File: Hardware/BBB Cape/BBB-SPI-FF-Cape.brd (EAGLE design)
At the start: 72.1 x 90.2 mm, 10 parts

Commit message: created the images for the modela
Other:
- board size 72.1 x 90.2 mm -> 54.6 x 71.8 mm

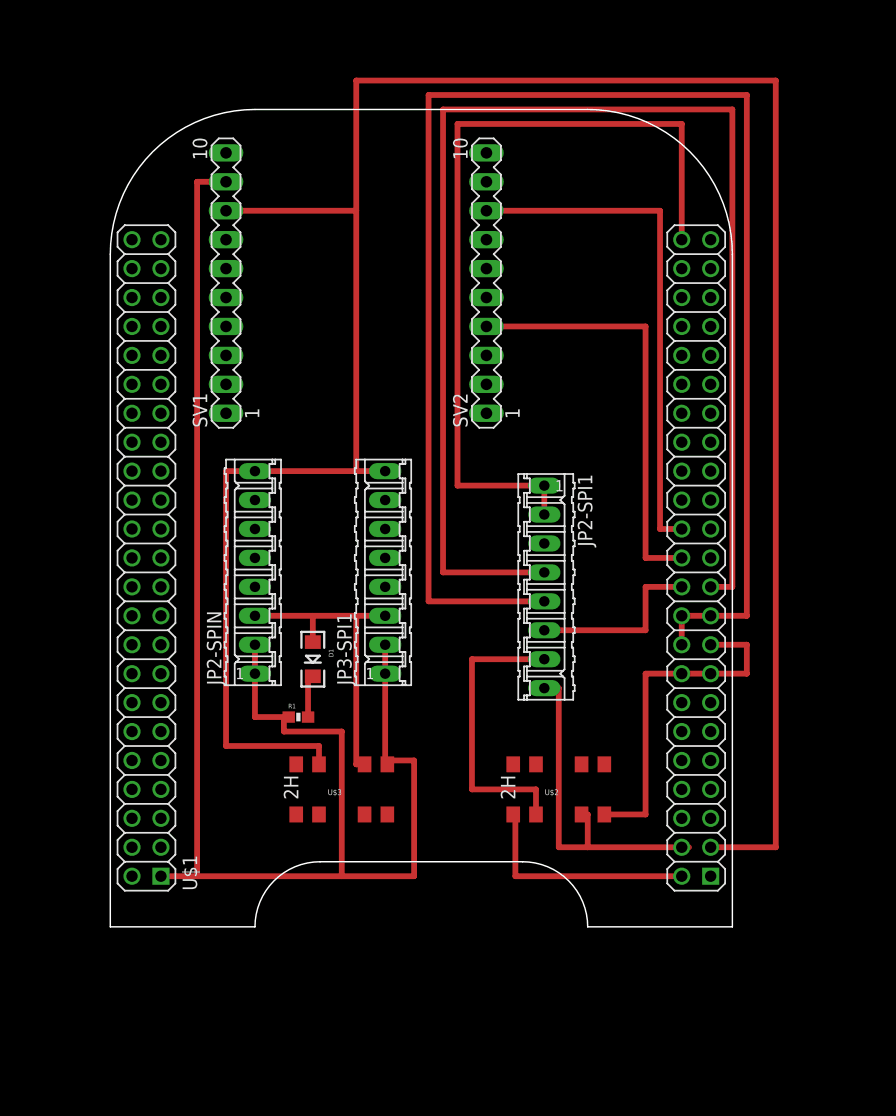
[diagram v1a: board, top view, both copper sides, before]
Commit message: Fixed the headers for the M08 cables coming from the IMU
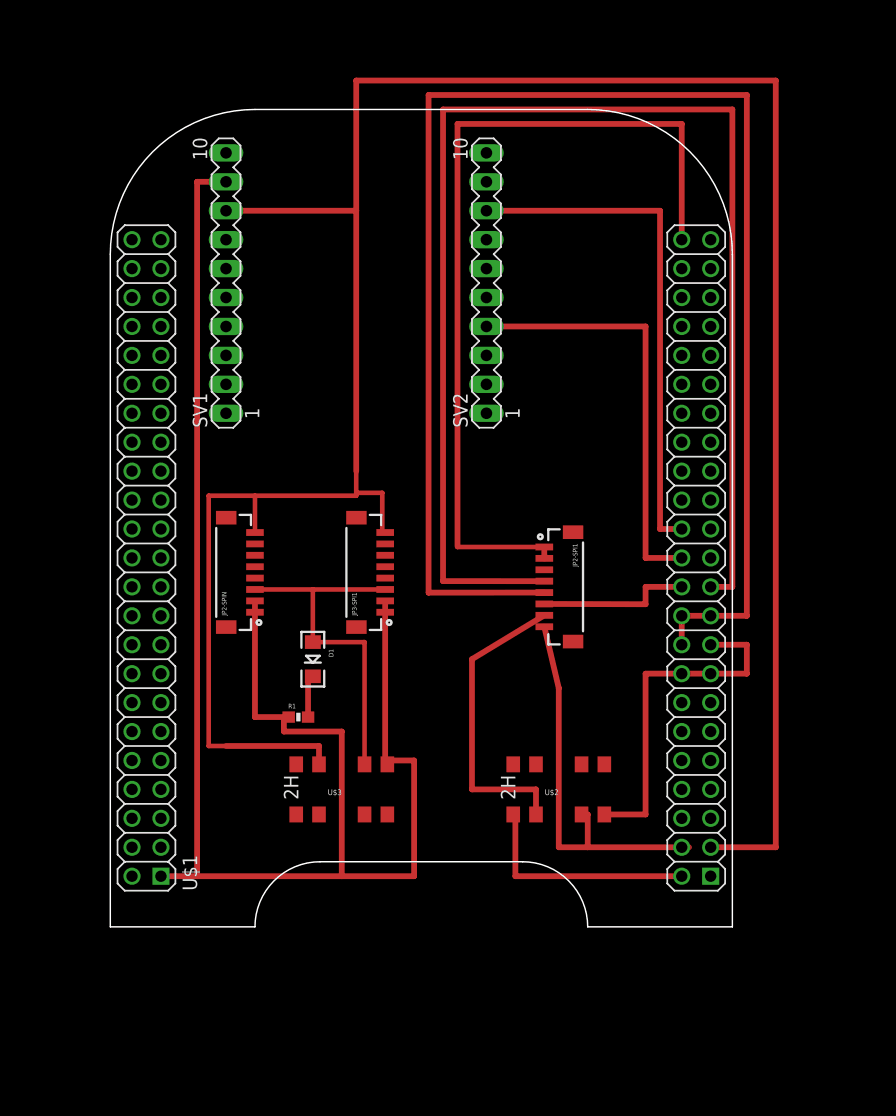
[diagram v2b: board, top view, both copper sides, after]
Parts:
- JP2-SPI1, JP2-SPIN, JP3-SPI1: device con-amp-quick:08P -> SparkFun-Connectors:BM08B-SRSS-TB
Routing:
- net GND: track 229.1 -> 240.7 mm
- net VCC: track 203.4 -> 213.2 mm
- net N$3: track 30.1 -> 34.4 mm
- net D: track 27.5 -> 31.3 mm
- net SCL: track 15.9 -> 13.6 mm
- net FF-CLK: track 25.9 -> 27.0 mm
- net SDO: track 118.7 -> 119.5 mm
- net SDA: track 136.5 -> 135.8 mm

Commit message: Cleaned up some of the traces
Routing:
- net FF-CLK: track 27.0 -> 29.8 mm
- net N$3: track 34.4 -> 35.5 mm
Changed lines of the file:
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@@
 <contactref element="JP2-SPI1" pad="8"/>
 <contactref element="U$2" pad="6"/>
-<wire x1="45.72" y1="39.68" x2="46.99" y2="34.29" width="0.508" layer="1"/>
 <wire x1="46.99" y1="34.29" x2="46.99" y2="20.32" width="0.508" layer="1"/>
 <wire x1="46.99" y1="20.32" x2="49.53" y2="20.32" width="0.508" layer="1"/>
@@
 <wire x1="48.99" y1="23.2" x2="49.53" y2="23.2" width="0.508" layer="1"/>
 <wire x1="49.53" y1="23.2" x2="49.53" y2="20.32" width="0.508" layer="1"/>
+<wire x1="45.72" y1="39.68" x2="45.72" y2="34.417" width="0.4064" layer="1"/>
+<wire x1="45.72" y1="34.417" x2="46.99" y2="34.417" width="0.4064" layer="1"/>
+<wire x1="46.99" y1="34.417" x2="46.99" y2="34.29" width="0.4064" layer="1"/>
 </signal>
 <signal name="D">
@@
 <contactref element="U$2" pad="7"/>
 <wire x1="44.99" y1="22.86" x2="44.99" y2="23.2" width="0.508" layer="1"/>
-<wire x1="45.72" y1="40.68" x2="39.37" y2="36.83" width="0.508" layer="1"/>
-<wire x1="39.37" y1="36.83" x2="39.37" y2="25.4" width="0.508" layer="1"/>
+<wire x1="45.72" y1="40.68" x2="39.37" y2="40.64" width="0.508" layer="1"/>
+<wire x1="39.37" y1="40.64" x2="39.37" y2="25.4" width="0.508" layer="1"/>
 <wire x1="39.37" y1="25.4" x2="44.99" y2="25.4" width="0.508" layer="1"/>
 <wire x1="45.72" y1="25.4" x2="44.99" y2="25.4" width="0" layer="19" extent="1-16"/>

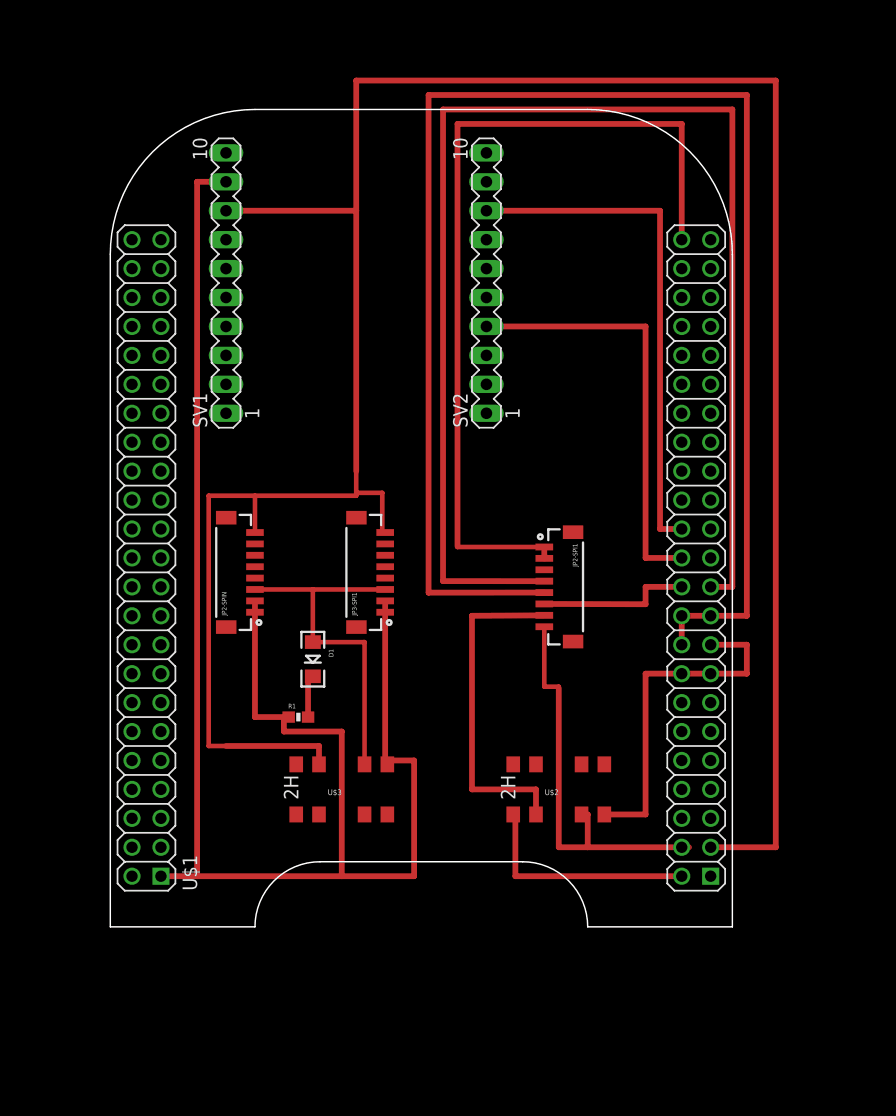
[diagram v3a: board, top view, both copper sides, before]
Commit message: Split cape into two components
Lower layer is the GPS and Pot and upper layer is the SPI connections
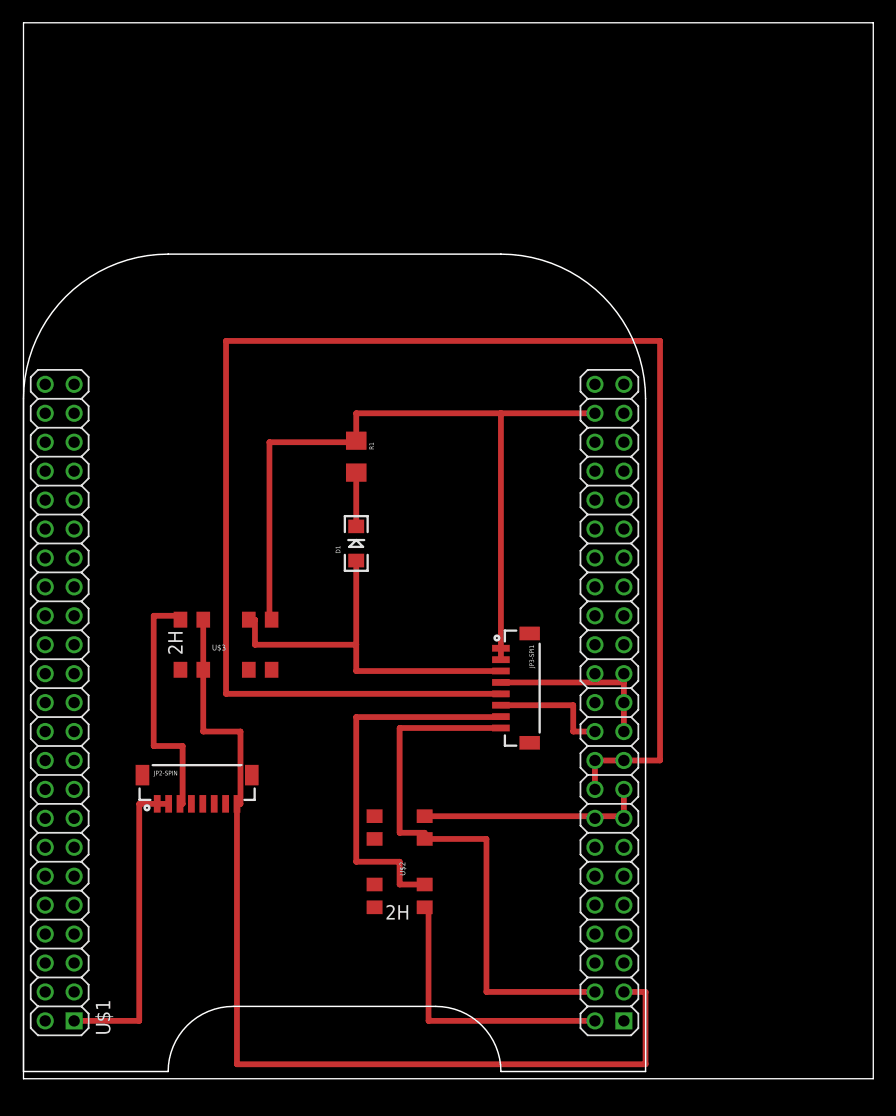
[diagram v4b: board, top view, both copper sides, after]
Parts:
- removed JP2-SPI1: (no value), SparkFun-Connectors:BM08B-SRSS-TB
- removed SV1, SV2: (no value), con-lstb:MA10-1
- R1: device SparkFun-Resistors:0603-RES -> SparkFun-Resistors:1206
- moved R1 23.4 mm to (29.2, 54.6), turned to 270 degrees
- moved JP2-SPIN 20.9 mm to (15.2, 24.1), turned to 0 degrees
- moved U$3 16.3 mm to (17.8, 38.1)
- moved U$2 15.3 mm to (33.0, 19.1), turned to 270 degrees
- moved U$1 14.8 mm to (0.00, -14.0)
- moved JP3-SPI1 14.4 mm to (41.9, 34.3), turned to 270 degrees
- moved D1 10.9 mm to (29.2, 47.0), turned to 90 degrees
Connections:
- removed net N$3: JP2-SPI1.8, U$2.6
- removed net VDD_3V3EXP: U$1.50
- new net AIN1: U$1.86
- new net AIN2: U$1.83
- new net AIN4: U$1.79
- new net AIN6: U$1.81
- new net Q: JP2-SPIN.3, U$3.4
- net D: no longer JP2-SPIN.3
- net FF-CLK: now also JP3-SPI1.7; no longer JP2-SPI1.7
- net GND: no longer JP2-SPI1.1, JP2-SPI1.2, SV1.9
- net RX-B: no longer SV2.4
- net SCL: now also JP3-SPI1.6; no longer JP2-SPI1.6
- net SDA: now also JP3-SPI1.5; no longer JP2-SPI1.5
- net SDO: now also JP3-SPI1.4; no longer JP2-SPI1.4
- net TX-B: no longer SV2.8
- net VCC: now also U$1.50, U$2.6; no longer SV1.8
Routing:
- net GND: track 240.7 -> 120.8 mm
- net SDO: track 119.5 -> 15.1 mm
- net VCC: track 213.2 -> 135.9 mm
- net TX-B: track 45.1 -> 0.00 mm
- net RX-B: track 37.5 -> 0.00 mm
- net N$3: track 35.5 -> 0.00 mm
- net Q: track 0.00 -> 22.0 mm
- net CS: track 30.6 -> 19.8 mm
- net FF-CLK: track 29.8 -> 33.4 mm
- net SCL: track 13.6 -> 10.6 mm
- net D: track 31.3 -> 34.0 mm
- net SDA: track 135.8 -> 138.3 mm
- net N$1: track 4.00 -> 4.72 mm
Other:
- board size 54.6 x 71.8 mm -> 74.6 x 92.7 mm
